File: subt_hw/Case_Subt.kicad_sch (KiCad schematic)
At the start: 36 parts, among them J1 P2.00 01x04, J2 USB_C_Receptacle_USB2.0_14P, J3 Conn_01x02, U1 RP2040, U2 W25Q16JVUXIQ, U3 MT2492, U4 USBLC6-2SC6, Y1 12MHz

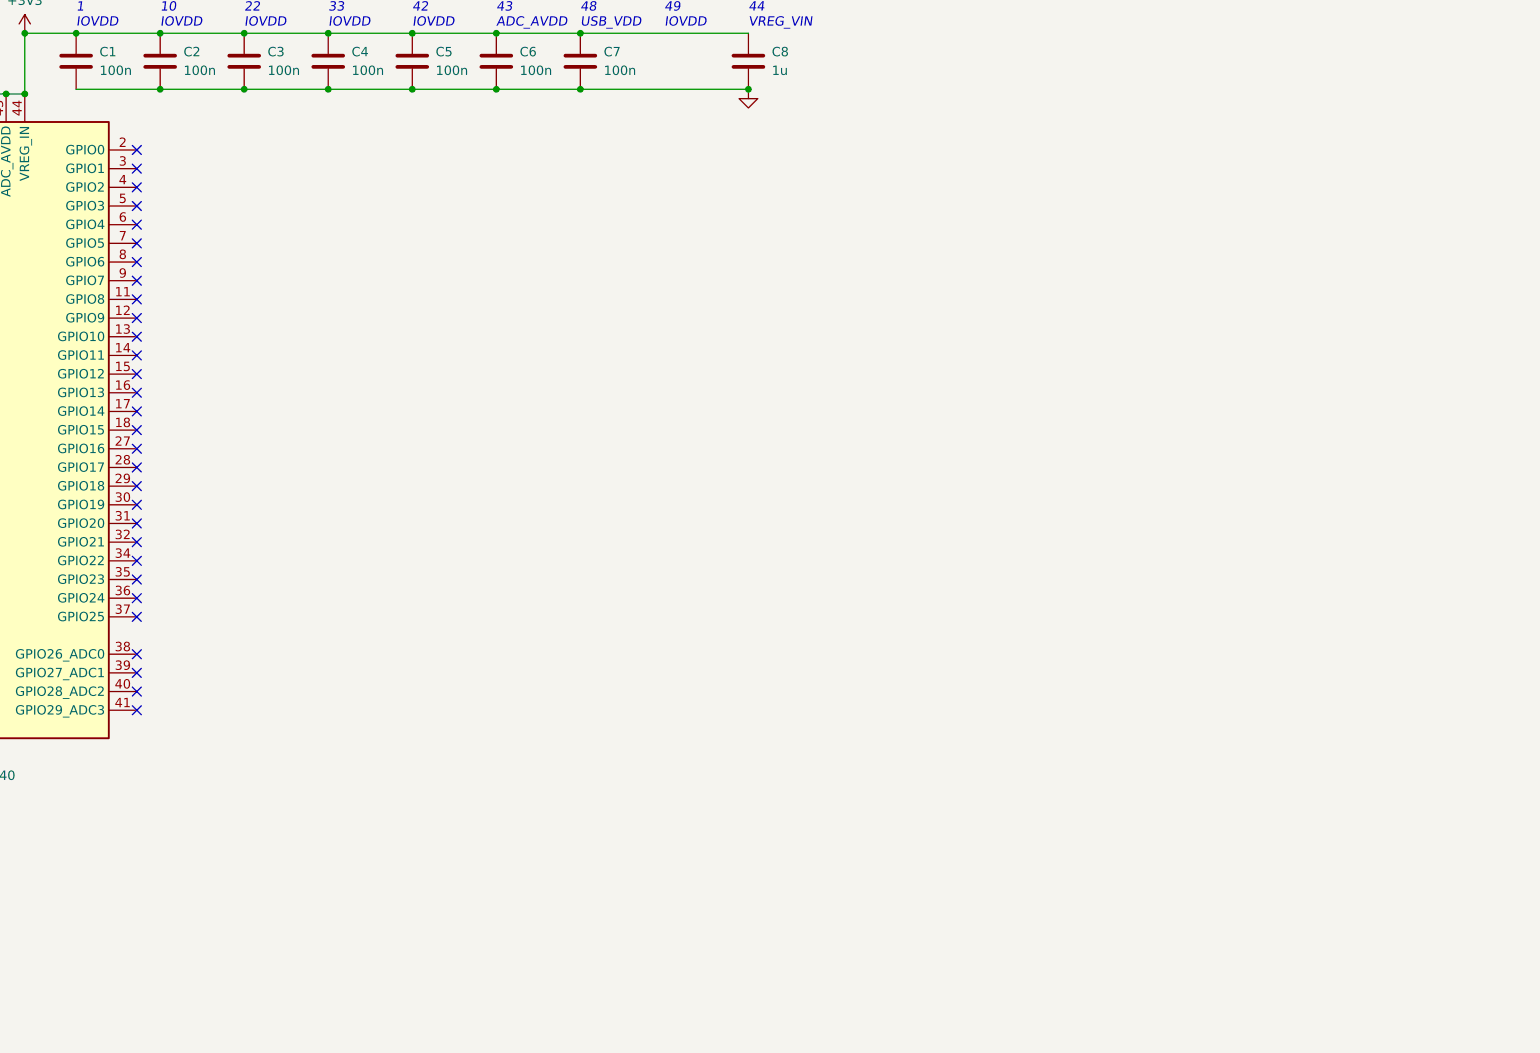
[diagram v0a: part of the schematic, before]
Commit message: Add all 16 ports
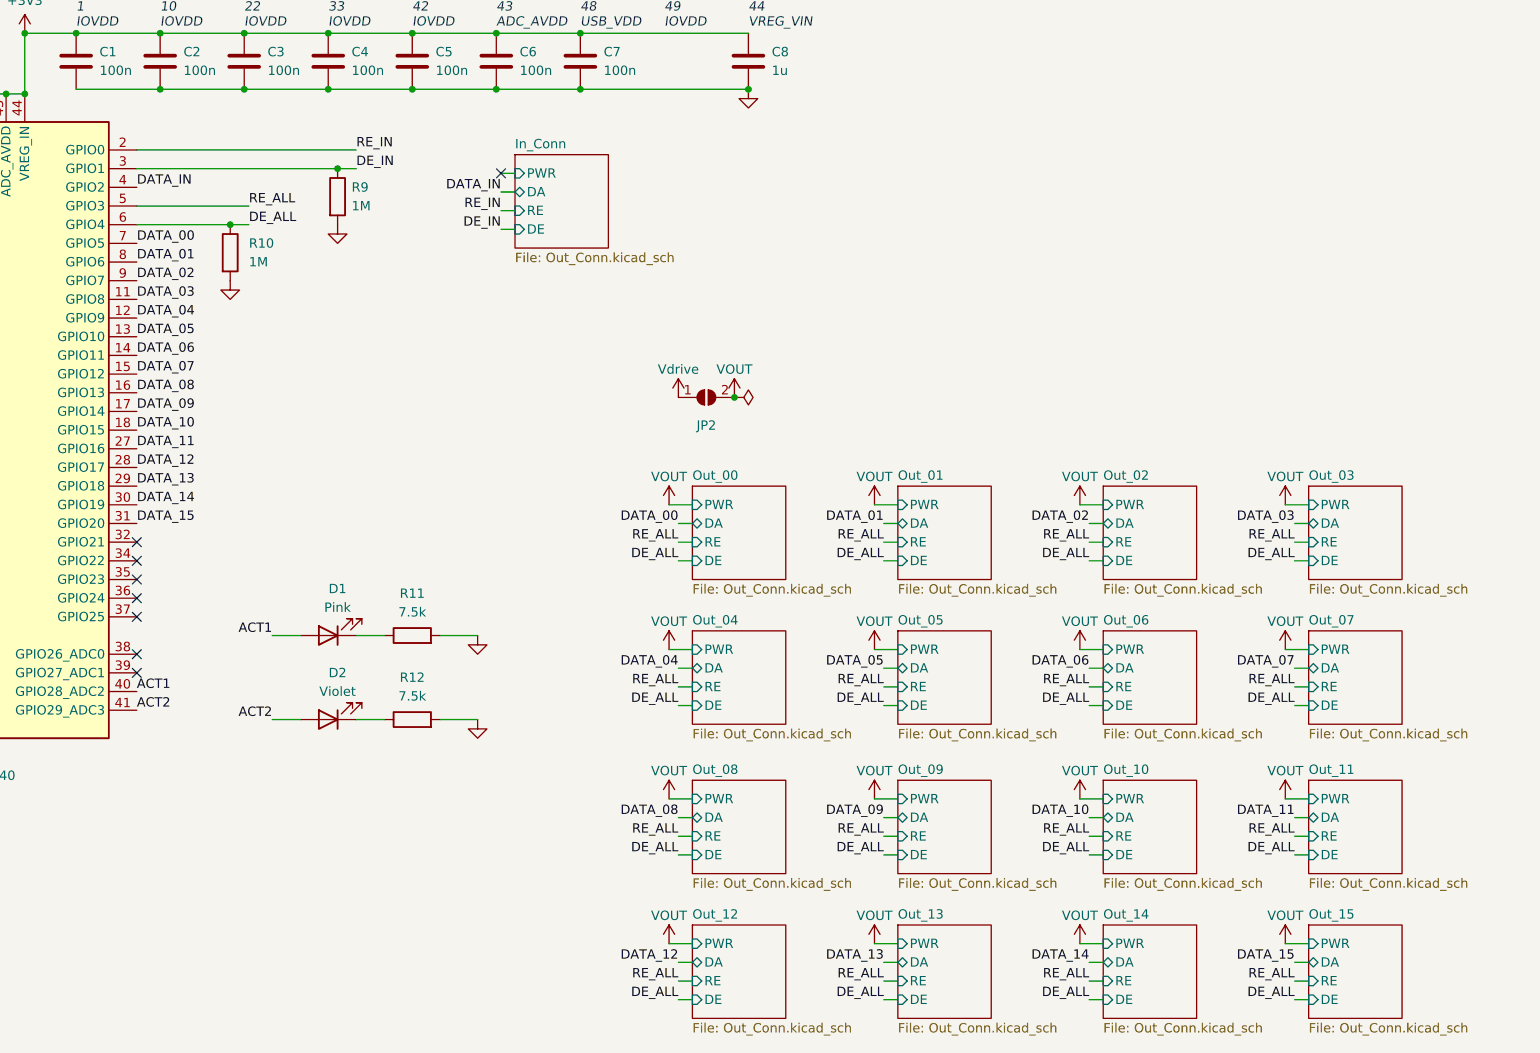
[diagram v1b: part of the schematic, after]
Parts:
- added D1: Pink, LED_SMD:LED_0603_1608Metric, symbol Device:LED
- added D2: Violet, LED_SMD:LED_0603_1608Metric, symbol Device:LED
- added JP2: SolderJumper_2_Open, Jumper:SolderJumper-2_P1.3mm_Open_RoundedPad1.0x1.5mm, symbol Jumper:SolderJumper_2_Open
- added R10, R9: 1M, Resistor_SMD:R_0402_1005Metric, symbol Device:R
- added R11, R12: 7.5k, Resistor_SMD:R_0402_1005Metric, symbol Device:R
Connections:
- net GND: now also R10.2, R11.2, R12.2, R9.2
- net Vdrive: now also JP2.1 (A)
- net DATA_03: now reaches U1.11 (GPIO8)
- net DATA_04: now reaches U1.12 (GPIO9)
- net DATA_05: now reaches U1.13 (GPIO10)
- net DATA_06: now reaches U1.14 (GPIO11)
- net DATA_07: now reaches U1.15 (GPIO12)
- net DATA_08: now reaches U1.16 (GPIO13)
- net DATA_09: now reaches U1.17 (GPIO14)
- net DATA_10: now reaches U1.18 (GPIO15)
- net RE_IN: now reaches U1.2 (GPIO0)
- net DATA_11: now reaches U1.27 (GPIO16)
- net DATA_12: now reaches U1.28 (GPIO17)
- net DATA_13: now reaches U1.29 (GPIO18)
- net DE_IN: now reaches U1.3 (GPIO1)
- net DE_IN: now also R9.1
- net DATA_14: now reaches U1.30 (GPIO19)
- net DATA_15: now reaches U1.31 (GPIO20)
- net DATA_IN: now reaches U1.4 (GPIO2)
- net ACT1: now reaches U1.40 (GPIO28_ADC2)
- net ACT1: now also D1.2 (A)
- net ACT2: now reaches U1.41 (GPIO29_ADC3)
- net ACT2: now also D2.2 (A)
- net RE_ALL: now reaches U1.5 (GPIO3)
- net DE_ALL: now reaches U1.6 (GPIO4)
- net DE_ALL: now also R10.1
- net DATA_00: now reaches U1.7 (GPIO5)
- net DATA_01: now reaches U1.8 (GPIO6)
- net DATA_02: now reaches U1.9 (GPIO7)
- new net: D2.1 (K), R12.1
- new net: D1.1 (K), R11.1
- new net VOUT: JP2.2 (B)
- no-connect marks 31 -> 9
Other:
- added sheet In_Conn (Out_Conn.kicad_sch)
- added sheet Out_00 (Out_Conn.kicad_sch)
- added sheet Out_01 (Out_Conn.kicad_sch)
- added sheet Out_02 (Out_Conn.kicad_sch)
- added sheet Out_03 (Out_Conn.kicad_sch)
- added sheet Out_04 (Out_Conn.kicad_sch)
- added sheet Out_05 (Out_Conn.kicad_sch)
- added sheet Out_06 (Out_Conn.kicad_sch)
- added sheet Out_07 (Out_Conn.kicad_sch)
- added sheet Out_08 (Out_Conn.kicad_sch)
- added sheet Out_09 (Out_Conn.kicad_sch)
- added sheet Out_10 (Out_Conn.kicad_sch)
- added sheet Out_11 (Out_Conn.kicad_sch)
- added sheet Out_12 (Out_Conn.kicad_sch)
- added sheet Out_13 (Out_Conn.kicad_sch)
- added sheet Out_14 (Out_Conn.kicad_sch)
- added sheet Out_15 (Out_Conn.kicad_sch)

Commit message: Simplify wiring
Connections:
- net RE_ALL is gone; now on net DATA_00: U1.5 (GPIO3)
- net RE_IN is gone; now on net DE_IN: U1.2 (GPIO0)
- net DATA_00: no longer U1.7 (GPIO5)
- net DATA_01: now also U1.6 (GPIO4); no longer U1.8 (GPIO6)
- net DATA_02: now also U1.7 (GPIO5); no longer U1.9 (GPIO7)
- net DATA_03: now also U1.8 (GPIO6); no longer U1.11 (GPIO8)
- net DATA_04: now also U1.9 (GPIO7); no longer U1.12 (GPIO9)
- net DATA_05: now also U1.11 (GPIO8); no longer U1.13 (GPIO10)
- net DATA_06: now also U1.12 (GPIO9); no longer U1.14 (GPIO11)
- net DATA_07: now also U1.13 (GPIO10); no longer U1.15 (GPIO12)
- net DATA_08: now also U1.14 (GPIO11); no longer U1.16 (GPIO13)
- net DATA_09: now also U1.15 (GPIO12); no longer U1.17 (GPIO14)
- net DATA_10: now also U1.16 (GPIO13); no longer U1.18 (GPIO15)
- net DATA_11: now also U1.17 (GPIO14); no longer U1.27 (GPIO16)
- net DATA_12: now also U1.18 (GPIO15); no longer U1.28 (GPIO17)
- net DATA_13: now also U1.27 (GPIO16); no longer U1.29 (GPIO18)
- net DATA_14: now also U1.28 (GPIO17); no longer U1.30 (GPIO19)
- net DATA_15: now also U1.29 (GPIO18); no longer U1.31 (GPIO20)
- net DATA_IN: now also U1.3 (GPIO1); no longer U1.4 (GPIO2)
- net DE_ALL: now also U1.4 (GPIO2); no longer U1.6 (GPIO4)
- net DE_IN: no longer U1.3 (GPIO1)
- no-connect marks 9 -> 11
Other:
- sheet In_Conn: file Out_Conn.kicad_sch -> Port.kicad_sch
- sheet In_Conn ports: added none; removed RE
- sheet Out_00: file Out_Conn.kicad_sch -> Port.kicad_sch
- sheet Out_00 ports: added none; removed RE
- sheet Out_01: file Out_Conn.kicad_sch -> Port.kicad_sch
- sheet Out_01 ports: added none; removed RE
- sheet Out_02: file Out_Conn.kicad_sch -> Port.kicad_sch
- sheet Out_02 ports: added none; removed RE
- sheet Out_03: file Out_Conn.kicad_sch -> Port.kicad_sch
- sheet Out_03 ports: added none; removed RE
- sheet Out_04: file Out_Conn.kicad_sch -> Port.kicad_sch
- sheet Out_04 ports: added none; removed RE
- sheet Out_05: file Out_Conn.kicad_sch -> Port.kicad_sch
- sheet Out_05 ports: added none; removed RE
- sheet Out_06: file Out_Conn.kicad_sch -> Port.kicad_sch
- sheet Out_06 ports: added none; removed RE
- sheet Out_07: file Out_Conn.kicad_sch -> Port.kicad_sch
- sheet Out_07 ports: added none; removed RE
- sheet Out_08: file Out_Conn.kicad_sch -> Port.kicad_sch
- sheet Out_08 ports: added none; removed RE
- sheet Out_09: file Out_Conn.kicad_sch -> Port.kicad_sch
- sheet Out_09 ports: added none; removed RE
- sheet Out_10: file Out_Conn.kicad_sch -> Port.kicad_sch
- sheet Out_10 ports: added none; removed RE
- sheet Out_11: file Out_Conn.kicad_sch -> Port.kicad_sch
- sheet Out_11 ports: added none; removed RE
- sheet Out_12: file Out_Conn.kicad_sch -> Port.kicad_sch
- sheet Out_12 ports: added none; removed RE
- sheet Out_13: file Out_Conn.kicad_sch -> Port.kicad_sch
- sheet Out_13 ports: added none; removed RE
- sheet Out_14: file Out_Conn.kicad_sch -> Port.kicad_sch
- sheet Out_14 ports: added none; removed RE
- sheet Out_15: file Out_Conn.kicad_sch -> Port.kicad_sch
- sheet Out_15 ports: added none; removed RE
- moved on the sheet: R10, R9

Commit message: 🚧 Layout, without the final stretch
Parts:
- removed JP1: SolderJumper_3_Open, Jumper:SolderJumper-3_P1.3mm_Open_RoundedPad1.0x1.5mm, symbol Jumper:SolderJumper_3_Open
- removed JP2: SolderJumper_2_Open, Jumper:SolderJumper-2_P1.3mm_Open_RoundedPad1.0x1.5mm, symbol Jumper:SolderJumper_2_Open
- added C18: 4.7u, Capacitor_SMD:C_0402_1005Metric, symbol Device:C
- added C19: 10n, Capacitor_SMD:C_0402_1005Metric, symbol Device:C
- added U4: SPX3819M5-L-3-3, Package_TO_SOT_SMD:SOT-23-5, symbol Regulator_Linear:SPX3819M5-L-3-3
- renumbered C18 to C20, U4 to U5
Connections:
- net Vdrive is gone; now on net VIN: C15.1, U3.4 (EN), U3.5 (IN)
- net +3V3: now also C18.1, U4.5 (OUT); no longer C17.1, L1.2, R5.1
- net +5V: now also C17.1, L1.2, R5.1, U4.1 (IN), U4.3 (EN)
- net GND: now also C18.2, C19.2, U4.2 (GND)
- new net: C19.1, U4.4 (BP)

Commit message: Finish subtree/router board design
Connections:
- net DATA_16: now reaches U1.30 (GPIO19)
- no-connect marks 11 -> 10
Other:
- added sheet Out_16 (Port.kicad_sch)
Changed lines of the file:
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@@
   (junction (at 197.485 40.005) (diameter 0) (color 0 0 0 0)
   )
-  (junction (at 91.44 31.75) (diameter 0) (color 0 0 0 0)
-  )
   (junction (at 64.77 39.37) (diameter 0) (color 0 0 0 0)
   )
   (junction (at 195.58 53.34) (diameter 0) (color 0 0 0 0)
   )
-  (junction (at 26.035 39.37) (diameter 0) (color 0 0 0 0)
-  )
   (junction (at 243.205 32.385) (diameter 0) (color 0 0 0 0)
   )
@@
   (junction (at 47.625 73.025) (diameter 0) (color 0 0 0 0)
   )
+  (junction (at -85.725 63.5) (diameter 0) (color 0 0 0 0)
+  )
   (junction (at 186.055 32.385) (diameter 0) (color 0 0 0 0)
   )
@@
   (junction (at 122.555 40.005) (diameter 0) (color 0 0 0 0)
   )
-  (no_connect (at 182.88 96.52))
   (no_connect (at 182.88 111.76))
   (no_connect (at 182.88 99.06))
@@
     (stroke (width 0) (type default))
   )
+  (wire (pts (xy 340.36 168.275) (xy 342.265 168.275))
+    (stroke (width 0) (type default))
+  )
   (wire (pts (xy 145.415 32.385) (xy 152.4 32.385))
     (stroke (width 0) (type default))
@@
     (stroke (width 0) (type default))
   )
+  (wire (pts (xy 340.36 170.815) (xy 342.265 170.815))
+    (stroke (width 0) (type default))
+  )
   (wire (pts (xy -16.51 53.975) (xy -18.415 53.975))
     (stroke (width 0) (type default))
@@
     (stroke (width 0) (type default))
   )
+  (wire (pts (xy 339.09 165.735) (xy 342.265 165.735))
+    (stroke (width 0) (type default))
+  )
   (wire (pts (xy 26.035 31.75) (xy 31.115 31.75))
     (stroke (width 0) (type default))
@@
     (effects (font (size 1.27 1.27)) (justify left bottom))
   )
+  (label "DE_ALL" (at 340.36 170.815 180) (fields_autoplaced)
+    (effects (font (size 1.27 1.27)) (justify right bottom))
+  )
   (label "USB_RAW_D-" (at -16.51 53.975 0) (fields_autoplaced)
     (effects (font (size 1.27 1.27)) (justify left bottom))
@@
     (effects (font (size 1.27 1.27)) (justify right bottom))
   )
+  (label "DATA_16" (at 340.36 168.275 180) (fields_autoplaced)
+    (effects (font (size 1.27 1.27)) (justify right bottom))
+  )
   (label "DE_ALL" (at 340.36 101.6 180) (fields_autoplaced)
     (effects (font (size 1.27 1.27)) (justify right bottom))
@@
     (effects (font (size 1.27 1.27)) (justify left bottom))
   )
+  (label "DATA_16" (at 182.88 96.52 0) (fields_autoplaced)
+    (effects (font (size 1.27 1.27)) (justify left bottom))
+  )
   (label "DATA_08" (at 182.88 76.2 0) (fields_autoplaced)
     (effects (font (size 1.27 1.27)) (justify left bottom))
@@
     )
   )
-  (symbol (lib_id "power:PWR_FLAG") (at 26.035 31.75 90) (unit 1)
-    (in_bom yes) (on_board yes) (dnp no)
-    (property "Reference" "#FLG02" (at 24.13 31.75 0)
-      (effects (font (size 1.27 1.27)) hide)
-    )
-    (property "Value" "PWR_FLAG" (at 22.225 31.75 90)
-      (effects (font (size 1.27 1.27)) (justify left) hide)
-    )
-    (property "Footprint" "" (at 26.035 31.75 0)
-      (effects (font (size 1.27 1.27)) hide)
-    )
-    (property "Datasheet" "~" (at 26.035 31.75 0)
-      (effects (font (size 1.27 1.27)) hide)
-    )
-    (pin "1")
-    (instances
-      (project "Case_Subt"
-        (path "/0810a37e-e9ef-4885-b57d-da39e5c5f463"
-          (reference "#FLG02") (unit 1)
-        )
-      )
-    )
-  )
   (symbol (lib_id "Case_symbols:VIN") (at 252.095 81.915 0) (unit 1)
     (in_bom yes) (on_board yes) (dnp no)
@@
     )
   )
-  (symbol (lib_id "power:PWR_FLAG") (at 91.44 31.75 270) (unit 1)
-    (in_bom yes) (on_board yes) (dnp no)
-    (property "Reference" "#FLG01" (at 93.345 31.75 0)
-      (effects (font (size 1.27 1.27)) hide)
-    )
-    (property "Value" "PWR_FLAG" (at 95.25 31.75 90)
-      (effects (font (size 1.27 1.27)) (justify left) hide)
-    )
-    (property "Footprint" "" (at 91.44 31.75 0)
-      (effects (font (size 1.27 1.27)) hide)
-    )
-    (property "Datasheet" "~" (at 91.44 31.75 0)
-      (effects (font (size 1.27 1.27)) hide)
-    )
-    (pin "1")
-    (instances
-      (project "Case_Subt"
-        (path "/0810a37e-e9ef-4885-b57d-da39e5c5f463"
-          (reference "#FLG01") (unit 1)
-        )
-      )
-    )
-  )
   (symbol (lib_id "Device:R") (at -59.69 31.75 0) (mirror x) (unit 1)
     (in_bom yes) (on_board yes) (dnp no)
@@
     )
   )
+  (symbol (lib_id "Case_symbols:VOUT") (at 339.09 165.735 0) (unit 1)
+    (in_bom yes) (on_board yes) (dnp no)
+    (property "Reference" "#PWR061" (at 339.09 169.545 0)
+      (effects (font (size 1.27 1.27)) hide)
+    )
+    (property "Value" "VOUT" (at 339.09 161.925 0)
+      (effects (font (size 1.27 1.27)))
+    )
+    (property "Footprint" "" (at 339.09 165.735 0)
+      (effects (font (size 1.27 1.27)) hide)
+    )
+    (property "Datasheet" "" (at 339.09 165.735 0)
+      (effects (font (size 1.27 1.27)) hide)
+    )
+    (pin "1")
+    (instances
+      (project "Case_Subt"
+        (path "/0810a37e-e9ef-4885-b57d-da39e5c5f463"
+          (reference "#PWR061") (unit 1)
+        )
+      )
+    )
+  )
   (symbol (lib_id "Device:C") (at 92.71 93.98 90) (unit 1)
     (in_bom yes) (on_board yes) (dnp no)
@@
     )
   )
-  (symbol (lib_id "power:PWR_FLAG") (at 26.035 39.37 90) (unit 1)
+  (symbol (lib_id "power:PWR_FLAG") (at -85.725 63.5 270) (unit 1)
     (in_bom yes) (on_board yes) (dnp no)
-    (property "Reference" "#FLG03" (at 24.13 39.37 0)
+    (property "Reference" "#FLG03" (at -83.82 63.5 0)
       (effects (font (size 1.27 1.27)) hide)
     )
-    (property "Value" "PWR_FLAG" (at 22.225 39.37 90)
+    (property "Value" "PWR_FLAG" (at -81.915 63.5 90)
       (effects (font (size 1.27 1.27)) (justify left) hide)
     )
-    (property "Footprint" "" (at 26.035 39.37 0)
+    (property "Footprint" "" (at -85.725 63.5 0)
       (effects (font (size 1.27 1.27)) hide)
     )
-    (property "Datasheet" "~" (at 26.035 39.37 0)
+    (property "Datasheet" "~" (at -85.725 63.5 0)
       (effects (font (size 1.27 1.27)) hide)
     )
@@
       )
     )
+  )
+  (sheet (at 342.265 163.195) (size 12.7 10.16)
+    (stroke (width 0.1524) (type solid))
+    (fill (color 0 0 0 0.0000))
+    (property "Sheetname" "Out_16" (at 342.265 162.4834 0)
+      (effects (font (size 1.27 1.27)) (justify left bottom))
+    )
+    (property "Sheetfile" "Port.kicad_sch" (at 342.265 173.99 0)
+      (effects (font (size 1.27 1.27)) (justify left top))
+    )
+    (pin "DE" input (at 342.265 170.815 180)
+      (effects (font (size 1.27 1.27)) (justify left))
+    )
+    (pin "DA" bidirectional (at 342.265 168.275 180)
+      (effects (font (size 1.27 1.27)) (justify left))
+    )
+    (pin "PWR" input (at 342.265 165.735 180)
+      (effects (font (size 1.27 1.27)) (justify left))
+    )
+    (instances
+      (project "Case_Subt"
+        (path "/0810a37e-e9ef-4885-b57d-da39e5c5f463" (page "19"))
+      )
+    )
